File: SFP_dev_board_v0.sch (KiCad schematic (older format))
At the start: 31 parts, among them P1 CONN_02X10, P2 SFP CAGE

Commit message: power Ic added
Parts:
- added C? (x3): 22u 16V, symbol CP
- added C?: 0.1u 16V, Capacitors_SMD:C_0805_HandSoldering, symbol C
- added U?: LM7805_TO220, TO_SOT_Packages_THT:TO-220_Vertical, symbol LM7805_TO220
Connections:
- net labels added: +5V
- wire segments 101 -> 112
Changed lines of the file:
@@
 Text GLabel 6400 2300 0    60   Input ~ 0
 RLOS
+$Comp
+L LM7805_TO220 U?
+U 1 1 5A0FC860
+P 7400 3800
+F 0 "U?" H 7250 3925 50  0000 C CNN
+F 1 "LM7805_TO220" H 7400 3925 50  0000 L CNN
+F 2 "TO_SOT_Packages_THT:TO-220_Vertical" H 7400 4025 50  0001 C CIN
+F 3 "" H 7400 3750 50  0001 C CNN
+	1    7400 3800
+	1    0    0    -1
+$EndComp
+$Comp
+L CP C?
+U 1 1 5A0FC8F3
+P 6900 4100
+F 0 "C?" H 6925 4200 50  0000 L CNN
+F 1 "22u 16V" H 6950 3950 50  0000 L CNN
+F 2 "" H 6938 3950 50  0000 C CNN
+F 3 "" H 6900 4100 50  0000 C CNN
+	1    6900 4100
+	1    0    0    -1
+$EndComp
+$Comp
+L CP C?
+U 1 1 5A0FC9DE
+P 7900 4100
+F 0 "C?" H 7925 4200 50  0000 L CNN
+F 1 "22u 16V" H 7950 3950 50  0000 L CNN
+F 2 "" H 7938 3950 50  0000 C CNN
+F 3 "" H 7900 4100 50  0000 C CNN
+	1    7900 4100
+	1    0    0    -1
+$EndComp
+$Comp
+L C C?
+U 1 1 5A0FCA7A
+P 8350 4100
+F 0 "C?" H 8375 4200 50  0000 L CNN
+F 1 "0.1u 16V" V 8200 3950 50  0000 L CNN
+F 2 "Capacitors_SMD:C_0805_HandSoldering" H 8388 3950 50  0001 C CNN
+F 3 "" H 8350 4100 50  0000 C CNN
+	1    8350 4100
+	1    0    0    -1
+$EndComp
+Wire Wire Line
+	6900 3950 6900 3800
+Wire Wire Line
+	6600 3800 7100 3800
+Wire Wire Line
+	7700 3800 8550 3800
+Wire Wire Line
+	7900 3950 7900 3800
+Connection ~ 7900 3800
+Wire Wire Line
+	8350 3950 8350 3800
+Connection ~ 8350 3800
+Wire Wire Line
+	7900 4350 7900 4250
+Wire Wire Line
+	6900 4350 8350 4350
+Wire Wire Line
+	7400 4350 7400 4100
+Wire Wire Line
+	6900 4350 6900 4250
+Connection ~ 7400 4350
+Wire Wire Line
+	8350 4350 8350 4250
+Connection ~ 7900 4350
+Connection ~ 6900 3800
+Text GLabel 8550 3800 2    60   Output ~ 0
+3.3V
+Text GLabel 6050 1600 0    60   Output ~ 0
++5V
+Wire Wire Line
+	6550 1600 6050 1600
+Text GLabel 6600 3800 0    60   Output ~ 0
++5V
+$Comp
+L CP C?
+U 1 1 5A0FDCA9
+P 6800 5450
+F 0 "C?" H 6825 5550 50  0000 L CNN
+F 1 "22u 16V" H 6850 5300 50  0000 L CNN
+F 2 "" H 6838 5300 50  0000 C CNN
+F 3 "" H 6800 5450 50  0000 C CNN
+	1    6800 5450
+	1    0    0    -1
+$EndComp
 $EndSCHEMATC

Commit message: test3
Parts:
- removed C?: 22u 16V, symbol CP
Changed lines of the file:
@@
 Text GLabel 6600 3800 0    60   Output ~ 0
 +5V
-$Comp
-L CP C?
-U 1 1 5A0FDCA9
-P 6800 5450
-F 0 "C?" H 6825 5550 50  0000 L CNN
-F 1 "22u 16V" H 6850 5300 50  0000 L CNN
-F 2 "" H 6838 5300 50  0000 C CNN
-F 3 "" H 6800 5450 50  0000 C CNN
-	1    6800 5450
-	1    0    0    -1
-$EndComp
 $EndSCHEMATC

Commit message: SN65EPT22 added
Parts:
- removed C?: 22u 16V, symbol CP
- removed U?: LM7805_TO220, TO_SOT_Packages_THT:TO-220_Vertical, symbol LM7805_TO220
- added C?: 0.1u 16V, Capacitors_SMD:C_0805_HandSoldering, symbol C
- added U?: LD1117AV33, TO_SOT_Packages_THT:TO-220-3_Horizontal, symbol LM317_3PinPackage
- added U?: SN65EPT22, Housings_SOIC:SOIC-8_3.9x4.9mm_Pitch1.27mm, symbol SN65EPT22
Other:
- moved on the sheet: C?, JP1, JP2, JP3, JP4, JP5
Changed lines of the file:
@@
 L JUMPER JP1
 U 1 1 5A0F4069
-P 1600 6200
-F 0 "JP1" H 1600 6350 50  0000 C CNN
-F 1 "JUMPER" H 1600 6120 50  0000 C CNN
-F 2 "" H 1600 6200 50  0000 C CNN
-F 3 "" H 1600 6200 50  0000 C CNN
-	1    1600 6200
+P 10150 5100
+F 0 "JP1" H 10150 5250 50  0000 C CNN
+F 1 "JUMPER" H 10150 5020 50  0000 C CNN
+F 2 "" H 10150 5100 50  0000 C CNN
+F 3 "" H 10150 5100 50  0000 C CNN
+	1    10150 5100
 	1    0    0    -1
 $EndComp
@@
 L JUMPER3 JP2
 U 1 1 5A0F7511
-P 4650 5600
-F 0 "JP2" H 4700 5500 50  0000 L CNN
-F 1 "JUMPER3" H 4650 5700 50  0000 C BNN
-F 2 "" H 4650 5600 50  0000 C CNN
-F 3 "" H 4650 5600 50  0000 C CNN
-	1    4650 5600
+P 1350 6000
+F 0 "JP2" H 1300 6150 50  0000 L CNN
+F 1 "JUMPER3" H 1350 6100 50  0001 C BNN
+F 2 "" H 1350 6000 50  0000 C CNN
+F 3 "" H 1350 6000 50  0000 C CNN
+	1    1350 6000
 	1    0    0    -1
 $EndComp
@@
 L JUMPER3 JP3
 U 1 1 5A0F7756
-P 4650 6000
-F 0 "JP3" H 4700 5900 50  0000 L CNN
-F 1 "JUMPER3" H 4650 6100 50  0000 C BNN
-F 2 "" H 4650 6000 50  0000 C CNN
-F 3 "" H 4650 6000 50  0000 C CNN
-	1    4650 6000
+P 1350 6400
+F 0 "JP3" H 1300 6550 50  0000 L CNN
+F 1 "JUMPER3" H 1350 6500 50  0001 C BNN
+F 2 "" H 1350 6400 50  0000 C CNN
+F 3 "" H 1350 6400 50  0000 C CNN
+	1    1350 6400
 	1    0    0    -1
 $EndComp
@@
 L JUMPER3 JP4
 U 1 1 5A0F77B7
-P 4650 6400
-F 0 "JP4" H 4700 6300 50  0000 L CNN
-F 1 "JUMPER3" H 4650 6500 50  0000 C BNN
-F 2 "" H 4650 6400 50  0000 C CNN
-F 3 "" H 4650 6400 50  0000 C CNN
-	1    4650 6400
+P 1350 6800
+F 0 "JP4" H 1300 6950 50  0000 L CNN
+F 1 "JUMPER3" H 1350 6900 50  0001 C BNN
+F 2 "" H 1350 6800 50  0000 C CNN
+F 3 "" H 1350 6800 50  0000 C CNN
+	1    1350 6800
 	1    0    0    -1
 $EndComp
@@
 L JUMPER3 JP5
 U 1 1 5A0F7825
-P 4650 6800
-F 0 "JP5" H 4700 6700 50  0000 L CNN
-F 1 "JUMPER3" H 4650 6900 50  0000 C BNN
-F 2 "" H 4650 6800 50  0000 C CNN
-F 3 "" H 4650 6800 50  0000 C CNN
-	1    4650 6800
+P 1350 7200
+F 0 "JP5" H 1300 7350 50  0000 L CNN
+F 1 "JUMPER3" H 1350 7300 50  0001 C BNN
+F 2 "" H 1350 7200 50  0000 C CNN
+F 3 "" H 1350 7200 50  0000 C CNN
+	1    1350 7200
 	1    0    0    -1
 $EndComp
@@
 RLOS
 $Comp
-L LM7805_TO220 U?
-U 1 1 5A0FC860
-P 7400 3800
-F 0 "U?" H 7250 3925 50  0000 C CNN
-F 1 "LM7805_TO220" H 7400 3925 50  0000 L CNN
-F 2 "TO_SOT_Packages_THT:TO-220_Vertical" H 7400 4025 50  0001 C CIN
-F 3 "" H 7400 3750 50  0001 C CNN
-	1    7400 3800
-	1    0    0    -1
-$EndComp
-$Comp
-L CP C?
-U 1 1 5A0FC8F3
-P 6900 4100
-F 0 "C?" H 6925 4200 50  0000 L CNN
-F 1 "22u 16V" H 6950 3950 50  0000 L CNN
-F 2 "" H 6938 3950 50  0000 C CNN
-F 3 "" H 6900 4100 50  0000 C CNN
-	1    6900 4100
-	1    0    0    -1
-$EndComp
-$Comp
 L CP C?
 U 1 1 5A0FC9DE
-P 7900 4100
-F 0 "C?" H 7925 4200 50  0000 L CNN
-F 1 "22u 16V" H 7950 3950 50  0000 L CNN
-F 2 "" H 7938 3950 50  0000 C CNN
-F 3 "" H 7900 4100 50  0000 C CNN
-	1    7900 4100
+P 4450 6250
+F 0 "C?" H 4475 6350 50  0000 L CNN
+F 1 "22u 16V" H 4500 6100 50  0000 L CNN
+F 2 "" H 4488 6100 50  0000 C CNN
+F 3 "" H 4450 6250 50  0000 C CNN
+	1    4450 6250
 	1    0    0    -1
 $EndComp
@@
 L C C?
 U 1 1 5A0FCA7A
-P 8350 4100
-F 0 "C?" H 8375 4200 50  0000 L CNN
-F 1 "0.1u 16V" V 8200 3950 50  0000 L CNN
-F 2 "Capacitors_SMD:C_0805_HandSoldering" H 8388 3950 50  0001 C CNN
-F 3 "" H 8350 4100 50  0000 C CNN
-	1    8350 4100
-	1    0    0    -1
-$EndComp
-Wire Wire Line
-	6900 3950 6900 3800
-Wire Wire Line
-	6600 3800 7100 3800
-Wire Wire Line
-	7700 3800 8550 3800
-Wire Wire Line
-	7900 3950 7900 3800
-Connection ~ 7900 3800
-Wire Wire Line
-	8350 3950 8350 3800
-Connection ~ 8350 3800
-Wire Wire Line
-	7900 4350 7900 4250
-Wire Wire Line
-	6900 4350 8350 4350
-Wire Wire Line
-	7400 4350 7400 4100
-Wire Wire Line
-	6900 4350 6900 4250
-Connection ~ 7400 4350
-Wire Wire Line
-	8350 4350 8350 4250
-Connection ~ 7900 4350
-Connection ~ 6900 3800
-Text GLabel 8550 3800 2    60   Output ~ 0
+P 4900 6250
+F 0 "C?" H 4925 6350 50  0000 L CNN
+F 1 "0.1u 16V" V 4750 6100 50  0000 L CNN
+F 2 "Capacitors_SMD:C_0805_HandSoldering" H 4938 6100 50  0001 C CNN
+F 3 "" H 4900 6250 50  0000 C CNN
+	1    4900 6250
+	1    0    0    -1
+$EndComp
+Wire Wire Line
+	3450 6100 3450 5950
+Wire Wire Line
+	3150 5950 3650 5950
+Wire Wire Line
+	4250 5950 5100 5950
+Wire Wire Line
+	4450 6100 4450 5950
+Connection ~ 4450 5950
+Wire Wire Line
+	4900 6100 4900 5950
+Connection ~ 4900 5950
+Wire Wire Line
+	4450 6500 4450 6400
+Wire Wire Line
+	3450 6500 4900 6500
+Wire Wire Line
+	3950 6500 3950 6250
+Wire Wire Line
+	3450 6500 3450 6400
+Connection ~ 3950 6500
+Wire Wire Line
+	4900 6500 4900 6400
+Connection ~ 4450 6500
+Connection ~ 3450 5950
+Text GLabel 5100 5950 2    60   Output ~ 0
 3.3V
 Text GLabel 6050 1600 0    60   Output ~ 0
@@
 Wire Wire Line
 	6550 1600 6050 1600
-Text GLabel 6600 3800 0    60   Output ~ 0
+Text GLabel 3150 5950 0    60   Output ~ 0
 +5V
+$Comp
+L LM317_3PinPackage U?
+U 1 1 5A0FE324
+P 3950 5950
+F 0 "U?" H 3950 6200 50  0000 C CNN
+F 1 "LD1117AV33" H 3700 6100 50  0000 L CNN
+F 2 "TO_SOT_Packages_THT:TO-220-3_Horizontal" H 3950 6200 50  0001 C CIN
+F 3 "" H 3950 5950 50  0001 C CNN
+	1    3950 5950
+	1    0    0    -1
+$EndComp
+$Comp
+L C C?
+U 1 1 5A0FE6EA
+P 3450 6250
+F 0 "C?" H 3475 6350 50  0000 L CNN
+F 1 "0.1u 16V" V 3300 6100 50  0000 L CNN
+F 2 "Capacitors_SMD:C_0805_HandSoldering" H 3488 6100 50  0001 C CNN
+F 3 "" H 3450 6250 50  0000 C CNN
+	1    3450 6250
+	1    0    0    -1
+$EndComp
+$Comp
+L SN65EPT22 U?
+U 1 1 5A0FF5C9
+P 7500 3500
+F 0 "U?" H 7400 3900 50  0000 R CNN
+F 1 "SN65EPT22" H 7400 3800 50  0000 R CNN
+F 2 "Housings_SOIC:SOIC-8_3.9x4.9mm_Pitch1.27mm" H 7500 3000 50  0001 C CNN
+F 3 "" H 7400 3900 50  0001 C CNN
+	1    7500 3500
+	1    0    0    -1
+$EndComp
 $EndSCHEMATC

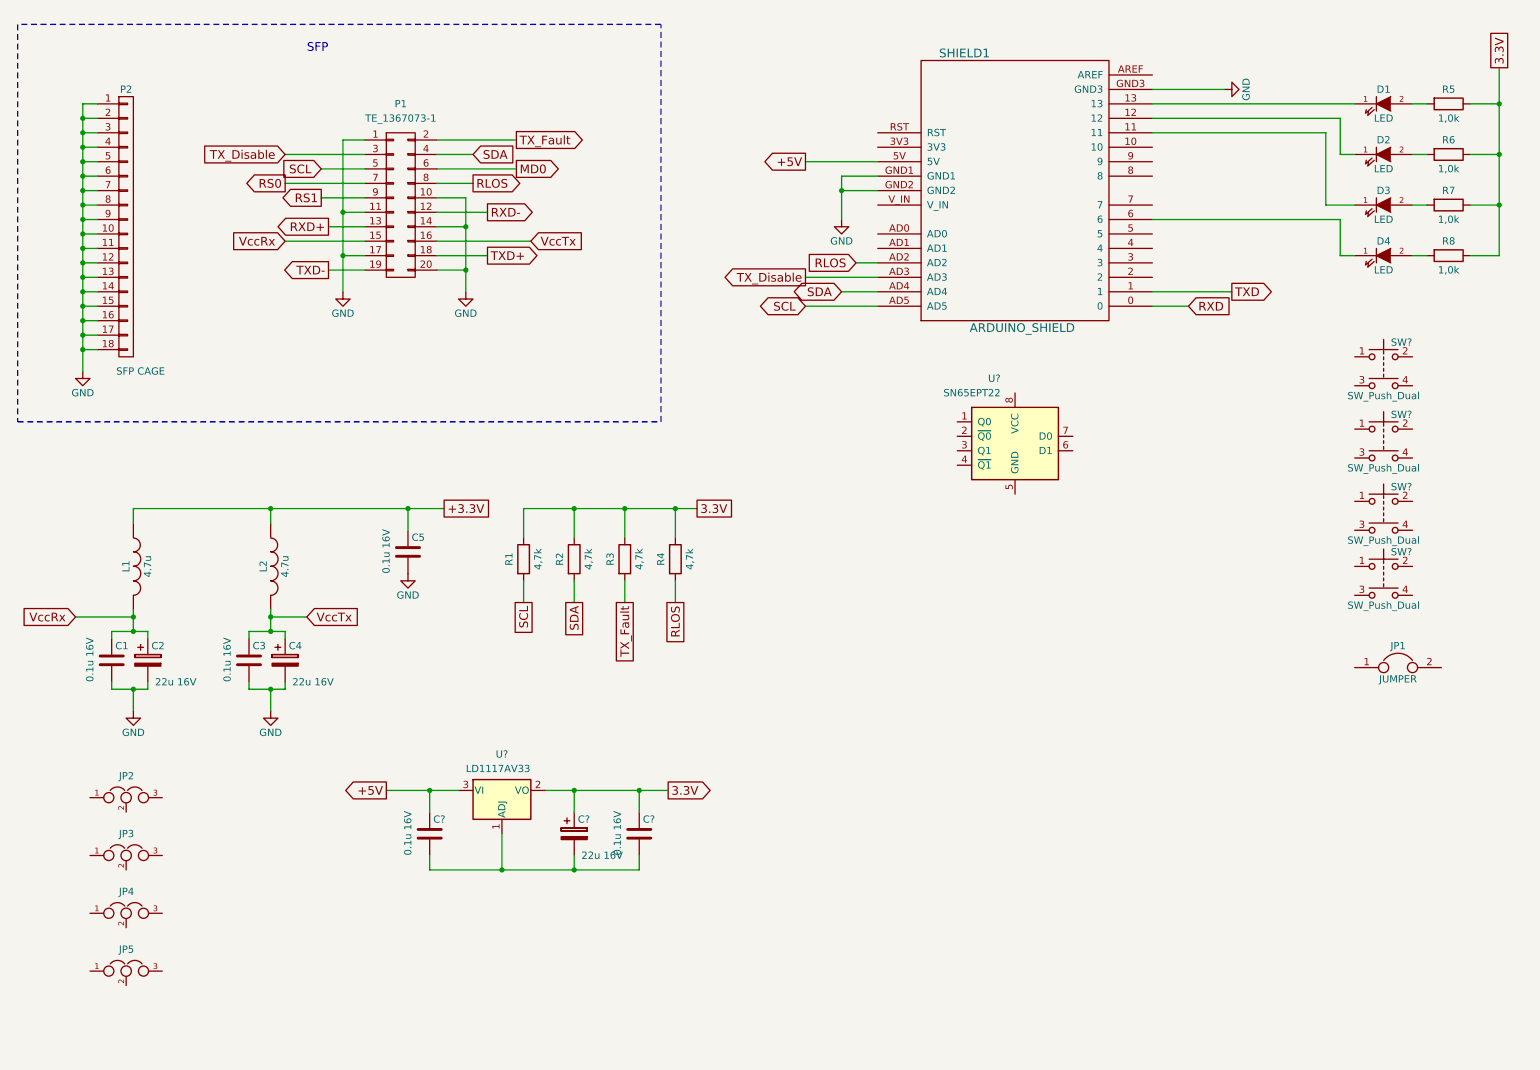
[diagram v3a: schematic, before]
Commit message: buffers added
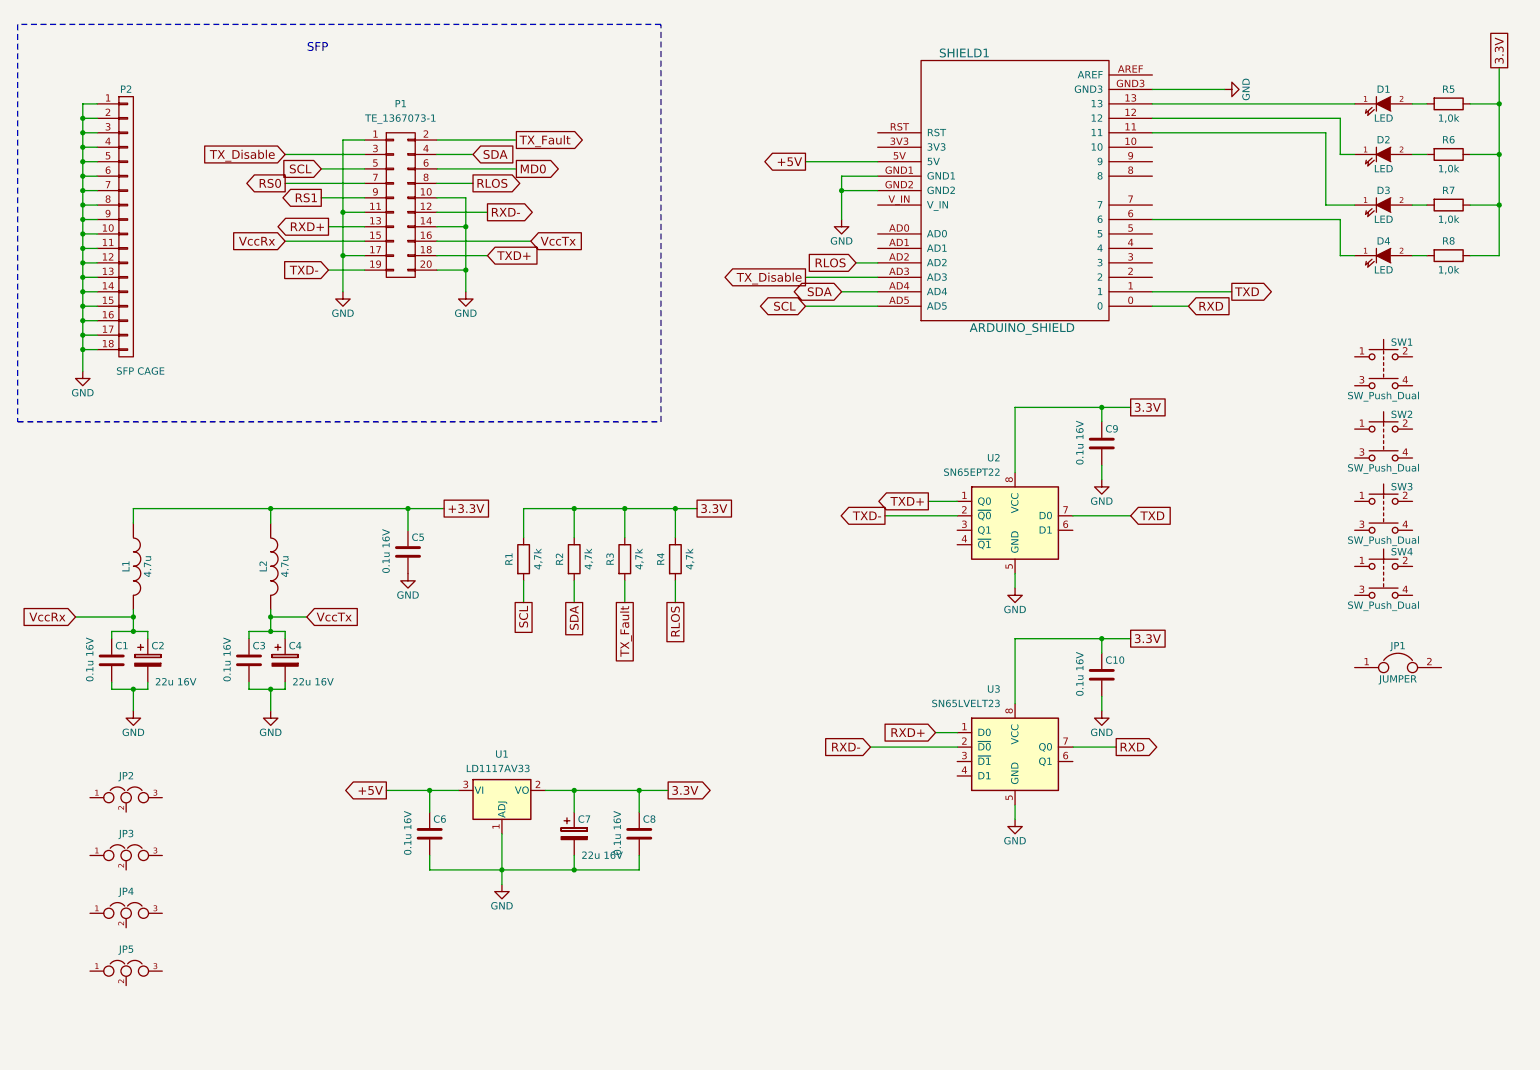
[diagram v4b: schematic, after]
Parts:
- added C10, C9: 0.1u 16V, Capacitors_SMD:C_0805_HandSoldering, symbol C
- added U3: SN65LVELT23, Housings_SOIC:SOIC-8_3.9x4.9mm_Pitch1.27mm, symbol SN65LVELT23
- gave numbers to parts that had none: 9
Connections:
- net 3.3V: now also U2.8 (VCC), C10.1, C9.1, U3.8 (VCC)
- net GND: now also C6.2, C7.2, C8.2, U1.1 (ADJ), U2.5 (GND), C10.2, C9.2, U3.5 (GND)
- net RXD: now also U3.7 (Q0)
- net RXD+: now also U3.1 (D0)
- net RXD-: now also U3.2 (~D0)
- net TXD: now also U2.7 (D0)
- net TXD+: now also U2.1 (Q0)
- net TXD-: now also U2.2 (~Q0)
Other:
- moved on the sheet: U2

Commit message: schematic complete
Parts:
- removed D1, D2, D3, D4: LED, LEDs:LED_0805_HandSoldering, symbol LED-RESCUE-SFP_dev_board_v0
- removed JP4, JP5: JUMPER3, symbol JUMPER3
- added D1, D2, D3, D4: LED, LEDs:LED_0805_HandSoldering, symbol LED
- added J1, J2: Conn_02x01_Row_Letter_First, Connectors_Samtec:SL-102-X-XX_1x02, symbol Conn_02x01_Row_Letter_First
- added R10, R9: 50, Resistors_SMD:R_0603_HandSoldering, symbol R
- added R11: 2k0, Resistors_SMD:R_0603_HandSoldering, symbol R
- added R12: 1k0, Resistors_SMD:R_0603_HandSoldering, symbol R
- JP2, JP3: footprint (none) -> Connectors_Samtec:SL-103-X-XX_1x03
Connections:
- net labels added: Uref
- wire segments 128 -> 148
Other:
- moved on the sheet: C10, C9, JP1, JP2, JP3, SW1, SW2, SW3, SW4, U2, U3

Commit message: schematic complete
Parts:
- removed JP1: JUMPER, symbol JUMPER
- added JP4: JUMPER3, Connectors_Samtec:SL-103-X-XX_1x03, symbol JUMPER3
- added R? (x4): 10k, Resistors_SMD:R_0603_HandSoldering, symbol R
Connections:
- net labels added: BUT1, BUT2, BUT3, BUT4, Vin
- wire segments 148 -> 183
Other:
- moved on the sheet: C6, C7, C8, SW1, SW2, SW3, SW4, U1

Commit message: schematic complete
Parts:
- SW1, SW2, SW3, SW4: footprint (none) -> Buttons_Switches_THT:SW_PUSH_6mm
- gave numbers to parts that had none: 4
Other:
- moved on the sheet: C1, C10, C2, C3, C4, C5, C6, C7, C8, C9, J1, J2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

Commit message: buffers
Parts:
- added C11, C12, C13, C14: 0.1u 16V, Capacitors_SMD:C_0805_HandSoldering, symbol C
- R10, R9: value 50 -> 120
- R11: value 2k0 -> 50
- R12: value 1k0 -> 50
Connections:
- net labels removed: Uref
- wire segments 183 -> 195
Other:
- moved on the sheet: R10, R9
